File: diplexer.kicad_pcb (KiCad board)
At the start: 2 copper layers, 157 x 72 mm, 27 parts, among them J1 Conn_Coaxial, J2 Conn_Coaxial, J3 Conn_Coaxial, J4 Conn_01x01_Pin, J5 Conn_01x01_Pin, J6 Conn_01x01_Pin, J7 Conn_01x01_Pin

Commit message: Add files via upload
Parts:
- added J10: Conn_01x01_Pin, MountingHole:MountingHole_3.2mm_M3_DIN965_Pad, F.Cu at (133.0, 65.0)
- added J11: Conn_01x01_Pin, MountingHole:MountingHole_3.2mm_M3_DIN965_Pad, F.Cu at (185.0, 65.0)
- added J8: Conn_01x01_Pin, MountingHole:MountingHole_3.2mm_M3_DIN965_Pad, F.Cu at (50.0, 65.0)
- added J9: Conn_01x01_Pin, MountingHole:MountingHole_3.2mm_M3_DIN965_Pad, F.Cu at (92.0, 65.0)
- J4, J5, J6, J7: footprint MountingHole:MountingHole_3.2mm_M3 -> MountingHole:MountingHole_3.2mm_M3_DIN965_Pad
- moved C9 20.6 mm to (137.0, 93.0), turned to 90 degrees
- moved L6 20.0 mm to (139.4, 83.0), turned to 0 degrees
- moved C7 20.0 mm to (86.0, 93.0), turned to 90 degrees
- moved C10 18.7 mm to (166.0, 93.5)
- moved C8 18.4 mm to (116.0, 93.0), turned to 90 degrees
- moved C6 16.6 mm to (67.0, 92.5), turned to 90 degrees
- moved C4 13.1 mm to (122.0, 53.4)
- moved L3 12.7 mm to (110.0, 53.6), turned to 90 degrees
- moved L8 10.3 mm to (91.0, 84.0)
- moved L5 9.56 mm to (151.0, 52.6), turned to 90 degrees
- moved L2 8.66 mm to (76.8, 43.4), turned to 0 degrees
- moved L9 8.34 mm to (77.0, 94.6), turned to 90 degrees
- moved L4 8.11 mm to (120.8, 43.4), turned to 0 degrees
- moved C5 7.75 mm to (139.0, 53.4)
- moved L7 7.72 mm to (127.0, 94.2), turned to 90 degrees
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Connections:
- C1 pad 1: Net-(J1-Ext) -> Net-(J1-In)
- J1 pad 1: GND -> Net-(J1-In)
- J1 pad 2: Net-(J1-Ext) -> GND
- J1 pad 3: (no net) -> GND
- J2 pad 3: (no net) -> GND
- J3 pad 3: (no net) -> GND
- L10 pad 1: Net-(J1-Ext) -> Net-(J1-In)
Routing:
- net Net-(J1-Ext): track 45.8 -> 0.00 mm
- net Net-(J1-In): track 0.00 -> 42.2 mm
- net Net-(C3-Pad2): track 15.4 -> 29.6 mm
- net Net-(C2-Pad2): track 12.4 -> 22.4 mm
- net Net-(J3-In): track 23.5 -> 33.1 mm
- net Net-(C6-Pad2): track 19.0 -> 25.9 mm
- net Net-(C8-Pad2): track 19.8 -> 26.3 mm
- net Net-(C4-Pad2): track 17.5 -> 23.4 mm
- net Net-(J2-In): track 41.2 -> 35.5 mm
- net Net-(C9-Pad2): track 24.5 -> 20.9 mm
- net Net-(C7-Pad2): track 18.3 -> 21.2 mm
- net Net-(C1-Pad2): track 16.7 -> 14.0 mm
- net GND: vias 96 -> 0
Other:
- board text added: "COPPER SHEAT AS SHIELD"
- board text added: "HF+6M lowpass and 4M highpass filter."

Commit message: Add files via upload
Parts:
- added REF**: KiCad-Logo2_8mm_SilkScreen, Symbol:KiCad-Logo2_8mm_SilkScreen, F.Cu at (168.0, 35.0)
- added REF**: OSHW-Logo2_14.6x12mm_SilkScreen, Symbol:OSHW-Logo2_14.6x12mm_SilkScreen, F.Cu at (164.0, 74.0)
- added REF**: Symbol_CreativeCommonsPublicDomain_SilkScreenTop_Small, Symbol:Symbol_CreativeCommonsPublicDomain_SilkScreenTop_Small, F.Cu at (88.0, 72.0)
- moved J9 4.00 mm to (96.0, 65.0)
- moved J10 1.00 mm to (134.0, 65.0)
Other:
- board text added: "1.5MM THICK"
- board text added: "15MM TALL"

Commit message: Add files via upload
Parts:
- moved C3 10.5 mm to (98.0, 53.4)
- moved C5 2.00 mm to (141.0, 53.4)
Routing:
- net Net-(C3-Pad2): track 29.6 -> 19.0 mm
- net Net-(C2-Pad2): track 22.4 -> 32.9 mm
- net Net-(J2-In): track 35.5 -> 33.5 mm
- net Net-(C4-Pad2): track 23.4 -> 25.4 mm
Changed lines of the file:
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@@
 	(footprint "Capacitor_SMD:C_2220_5750Metric"
 		(layer "F.Cu")
-		(at 139 53.44)
+		(at 141 53.44)
 		(descr "Capacitor SMD 2220 (5750 Metric), square (rectangular) end terminal, IPC-7351 nominal, (Body size from: http://datasheets.avx.com/AVX-HV_MLCC.pdf), generated with kicad-footprint-generator")
 		(tags "capacitor")
@@
 		(attr through_hole)
 		(fp_line
-			(start 18.28 -4.87)
+			(start 11.5 -4.87)
 			(end 2.04 -4.87)
 			(stroke
@@
 		)
 		(fp_line
-			(start 19.08 0)
-			(end 18.28 0)
+			(start 12.4 0)
+			(end 11.6 0)
 			(stroke
 				(width 0.12)
@@
 		)
 		(fp_line
-			(start 18.28 4.87)
-			(end 18.28 -4.87)
+			(start 11.5 4.87)
+			(end 11.5 -4.87)
 			(stroke
 				(width 0.12)
@@
 		(fp_line
 			(start 2.04 4.87)
-			(end 18.28 4.87)
-			(stroke
-				(width 0.12)
-				(type solid)
-			)
-			(layer "F.SilkS")
-		)
-		(fp_line
-			(start 21.57 -5)
+			(end 11.5 4.87)
+			(stroke
+				(width 0.12)
+				(type solid)
+			)
+			(layer "F.SilkS")
+		)
+		(fp_line
+			(start 16.5 -5)
 			(end -1.25 -5)
 			(stroke
@@
 		)
 		(fp_line
-			(start 21.57 5)
-			(end 21.57 -5)
+			(start 16.5 5)
+			(end 16.5 -5)
 			(stroke
 				(width 0.05)
@@
 		(fp_line
 			(start -1.25 5)
-			(end 21.57 5)
-			(stroke
-				(width 0.05)
-				(type solid)
-			)
-			(layer "F.CrtYd")
-		)
-		(fp_line
-			(start 18.16 -4.75)
+			(end 16.5 5)
+			(stroke
+				(width 0.05)
+				(type solid)
+			)
+			(layer "F.CrtYd")
+		)
+		(fp_line
+			(start 11.5 -4.75)
 			(end 2.16 -4.75)
 			(stroke
@@
 		)
 		(fp_line
-			(start 20.32 0)
-			(end 18.16 0)
+			(start 13.48 0)
+			(end 11.32 0)
 			(stroke
 				(width 0.1)
@@
 		)
 		(fp_line
-			(start 18.16 4.75)
-			(end 18.16 -4.75)
+			(start 11.5 4.75)
+			(end 11.5 -4.75)
 			(stroke
 				(width 0.1)
@@
 		(fp_line
 			(start 2.16 4.75)
-			(end 18.16 4.75)
+			(end 11.5 4.75)
 			(stroke
 				(width 0.1)
@@
 		(pad "1" thru_hole circle
 			(at 0 0 90)
-			(size 2 2)
-			(drill 1)
+			(size 3 3)
+			(drill 1.6)
 			(layers "*.Cu" "*.Mask")
 			(remove_unused_layers no)
@@
 	(footprint "Capacitor_SMD:C_2220_5750Metric"
 		(layer "F.Cu")
-		(at 87.45 53.44)
+		(at 98 53.44)
 		(descr "Capacitor SMD 2220 (5750 Metric), square (rectangular) end terminal, IPC-7351 nominal, (Body size from: http://datasheets.avx.com/AVX-HV_MLCC.pdf), generated with kicad-footprint-generator")
 		(tags "capacitor")
@@
 	)
 	(segment
-		(start 84.9 53.44)
-		(end 76.84 53.44)
-		(width 3)
-		(layer "F.Cu")
-		(net 3)
-	)
-	(segment
 		(start 76.84 53.44)
 		(end 72.55 53.44)
+		(width 3)
+		(layer "F.Cu")
+		(net 3)
+	)
+	(segment
+		(start 95.45 53.44)
+		(end 76.84 53.44)
 		(width 3)
 		(layer "F.Cu")
@@
 	)
 	(segment
+		(start 100.55 53.44)
+		(end 109.84 53.44)
+		(width 3)
+		(layer "F.Cu")
+		(net 4)
+	)
+	(segment
 		(start 119.29 53.6)
 		(end 110 53.6)
@@
 	)
 	(segment
-		(start 110 53.6)
-		(end 90.16 53.6)
-		(width 3)
-		(layer "F.Cu")
-		(net 4)
-	)
-	(segment
-		(start 90.16 53.6)
-		(end 90 53.44)
+		(start 109.84 53.44)
+		(end 110 53.6)
 		(width 3)
 		(layer "F.Cu")
@@
 	)
 	(segment
-		(start 136.45 53.44)
-		(end 124.55 53.44)
-		(width 3)
-		(layer "F.Cu")
-		(net 5)
-	)
-	(segment
 		(start 124.55 47.15)
 		(end 120.84 43.44)
+		(width 3)
+		(layer "F.Cu")
+		(net 5)
+	)
+	(segment
+		(start 138.45 53.44)
+		(end 124.55 53.44)
 		(width 3)
 		(layer "F.Cu")
@@
 	)
 	(segment
+		(start 143.55 53.44)
+		(end 144.39 52.6)
+		(width 3)
+		(layer "F.Cu")
+		(net 6)
+	)
+	(segment
 		(start 151 52.6)
 		(end 169.4 52.6)
@@
 	)
 	(segment
-		(start 142.39 52.6)
+		(start 144.39 52.6)
 		(end 151 52.6)
 		(width 3)
 		(layer "F.Cu")
-		(net 6)
-	)
-	(segment
-		(start 141.55 53.44)
-		(end 142.39 52.6)
-		(width 3)
-		(layer "F.Cu")

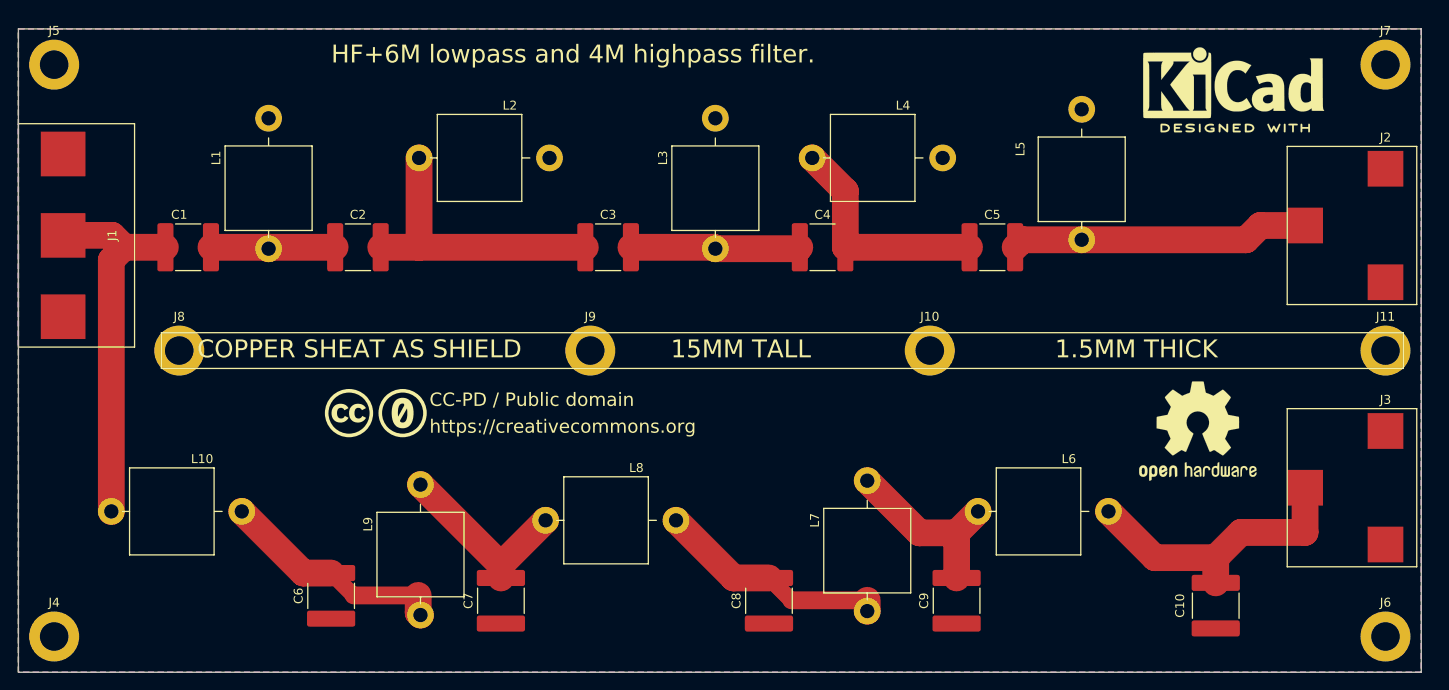
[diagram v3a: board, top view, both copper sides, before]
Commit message: Add files via upload
Updated capacitors foot prints to 2525 (QEEV Series)
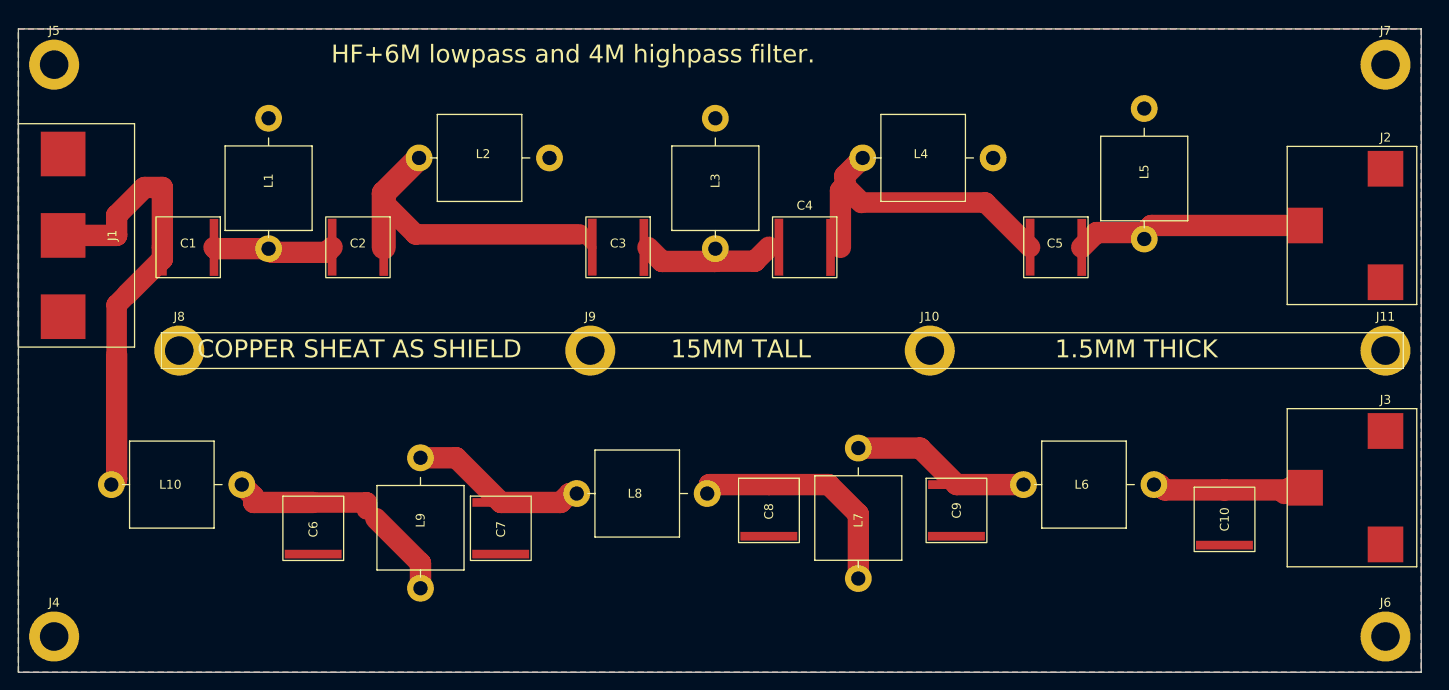
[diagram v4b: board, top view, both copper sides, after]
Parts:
- removed REF**: KiCad-Logo2_8mm_SilkScreen, Symbol:KiCad-Logo2_8mm_SilkScreen
- removed REF**: OSHW-Logo2_14.6x12mm_SilkScreen, Symbol:OSHW-Logo2_14.6x12mm_SilkScreen
- removed REF**: Symbol_CreativeCommonsPublicDomain_SilkScreenTop_Small, Symbol:Symbol_CreativeCommonsPublicDomain_SilkScreenTop_Small
- C1, C10, C2, C3, C4, C5, C6, C7, C8, C9: footprint Capacitor_SMD:C_2220_5750Metric -> sparkfun-electromech:2525
- moved C9 10.1 mm to (137.0, 82.9), turned to 0 degrees
- moved C8 10.1 mm to (116.0, 82.9), turned to 0 degrees
- moved C10 9.71 mm to (167.0, 83.9), turned to 0 degrees
- moved C7 8.11 mm to (86.0, 84.9), turned to 0 degrees
- moved C6 7.82 mm to (65.0, 84.9), turned to 0 degrees
- moved C5 7.11 mm to (148.1, 53.4), turned to -90 degrees
- moved L5 7.00 mm to (158.0, 52.5)
- moved L6 5.91 mm to (144.5, 80.0)
- moved L4 5.65 mm to (126.5, 43.4)
- moved L8 4.60 mm to (94.5, 81.0)
- moved L7 3.78 mm to (126.0, 90.5)
- moved L10 3.00 mm to (42.4, 80.0)
- moved L9 3.00 mm to (77.0, 91.6)
- moved C4 2.00 mm to (120.0, 53.4), turned to -90 degrees
- moved C3 1.11 mm to (99.1, 53.4), turned to -90 degrees
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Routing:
- net Net-(J3-In): track 33.1 -> 17.4 mm
- net Net-(C4-Pad2): track 25.4 -> 34.6 mm
- net Net-(J1-In): track 42.2 -> 50.3 mm
- net Net-(J2-In): track 33.5 -> 26.7 mm
- net Net-(C2-Pad2): track 32.9 -> 37.0 mm
- net Net-(C3-Pad2): track 19.0 -> 16.3 mm
- net Net-(C6-Pad2): track 25.9 -> 27.3 mm
- net Net-(C7-Pad2): track 21.2 -> 20.0 mm
- net Net-(C9-Pad2): track 20.9 -> 20.2 mm

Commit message: Add files via upload
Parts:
- added C11: 30pF, sparkfun-electromech:1111, F.Cu at (51.2, 48.1)
- added C12: 12pF, sparkfun-electromech:1111, F.Cu at (70.0, 48.0)
- added C13: 12pF, sparkfun-electromech:1111, F.Cu at (99.0, 48.0)
- added C14: 12pF, sparkfun-electromech:1111, F.Cu at (120.0, 48.0)
- added C15: 10pF, sparkfun-electromech:1111, F.Cu at (148.0, 49.0)
- added C16: 16pF, sparkfun-electromech:1111, F.Cu at (69.0, 86.0)
- added C17: 10pF, sparkfun-electromech:1111, F.Cu at (91.0, 86.0)
- added C18: 10pF, sparkfun-electromech:1111, F.Cu at (120.0, 84.0)
- added C19: 10pF, sparkfun-electromech:1111, F.Cu at (141.0, 84.0)
- added C20: 22pF, sparkfun-electromech:1111, F.Cu at (170.5, 83.5)
- C1: value 43pF -> 13pF; footprint sparkfun-electromech:2525 -> sparkfun-electromech:1111
- C10: value 62pF -> 39pF; footprint sparkfun-electromech:2525 -> sparkfun-electromech:1111
- C2, C4: value 24pF -> 12pF; footprint sparkfun-electromech:2525 -> sparkfun-electromech:1111
- C3: value 24F -> 12pF; footprint sparkfun-electromech:2525 -> sparkfun-electromech:1111
- C5: value 30pF -> 20pF; footprint sparkfun-electromech:2525 -> sparkfun-electromech:1111
- C6: value 91pF -> 75pF; footprint sparkfun-electromech:2525 -> sparkfun-electromech:1111
- C7, C9: value 110pF -> 100pF; footprint sparkfun-electromech:2525 -> sparkfun-electromech:1111
- C8: value 110ppF -> 100pF; footprint sparkfun-electromech:2525 -> sparkfun-electromech:1111
- moved C10 3.75 mm to (163.5, 82.5)
- moved C6 2.90 mm to (62.1, 84.9)
- moved C8 2.00 mm to (114.0, 83.0)
- moved C9 1.99 mm to (135.0, 82.9)
- moved L7 1.50 mm to (127.5, 90.5)
- moved C7 0.89 mm to (85.1, 84.9)
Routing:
- net Net-(C13-Pad2): track 16.3 -> 30.0 mm
- net Net-(C1-Pad2): track 13.7 -> 26.0 mm
- net Net-(C12-Pad2): track 37.0 -> 45.6 mm
- net Net-(C14-Pad2): track 34.6 -> 40.9 mm
- net Net-(J2-In): track 26.7 -> 32.4 mm
- net Net-(J3-In): track 17.4 -> 22.9 mm
- net Net-(J1-In): track 50.3 -> 45.5 mm
- net Net-(C17-Pad1): track 20.0 -> 23.3 mm
- net Net-(C18-Pad1): track 26.3 -> 25.0 mm
- net Net-(C19-Pad1): track 20.2 -> 21.2 mm
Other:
- board text added: "100W MAX!"

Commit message: Add files via upload
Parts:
- J2: footprint sparkfun-electromech:N-conn slanted -> sparkfun-electromech:UHF slanted
- moved J2 1.90 mm to (184.0, 49.4), turned to 90 degrees
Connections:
- net Net-(J2-In) renamed /HF+6M
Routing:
- net /HF+6M: track 32.4 -> 41.1 mm

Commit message: Add files via upload
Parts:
- J2: footprint sparkfun-electromech:UHF slanted -> sparkfun-electromech:N-conn slanted
- J3: footprint sparkfun-electromech:N-conn slanted -> sparkfun-electromech:UHF slanted
- turned J2 to -90 degrees
- turned J3 to 90 degrees
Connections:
- net /HF+6M renamed Net-(J2-In)
- J1 pad 3: GND -> (no net)
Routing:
- net Net-(J3-In): track 22.9 -> 31.9 mm
- net Net-(J2-In): track 41.1 -> 32.1 mm
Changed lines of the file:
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@@
 	(net 10 "Net-(C18-Pad1)")
 	(net 11 "Net-(C19-Pad1)")
-	(net 12 "/HF+6M")
+	(net 12 "Net-(J2-In)")
 	(footprint "sparkfun-electromech:1111"
 		(layer "F.Cu")
@@
 		)
 	)
-	(footprint "sparkfun-electromech:N-conn slanted"
+	(footprint "sparkfun-electromech:UHF slanted"
 		(layer "F.Cu")
-		(at 185 80.35 -90)
+		(at 185 80.35 90)
+		(descr "UHF slanted")
 		(property "Reference" "J3"
-			(at -9.85 0 0)
+			(at 0 -5.5 90)
 			(layer "F.SilkS")
 			(effects
@@
 			)
 		)
-		(property "Footprint" "sparkfun-electromech:N-conn slanted"
+		(property "Footprint" "sparkfun-electromech:UHF slanted"
 			(at 0 0 90)
 			(layer "F.Fab")
@@
 		(attr smd)
 		(fp_line
-			(start -8.85 11)
-			(end -8.85 -3.5)
+			(start 12.5 -8)
+			(end -12.5 -8)
 			(stroke
 				(width 0.12)
@@
 		)
 		(fp_line
-			(start 8.85 11)
-			(end -8.85 11)
+			(start -12.5 -8)
+			(end -12.5 5)
 			(stroke
 				(width 0.12)
@@
 		)
 		(fp_line
-			(start -8.85 -3.5)
-			(end 8.85 -3.5)
+			(start 12.5 5)
+			(end 12.5 -8)
 			(stroke
 				(width 0.12)
@@
 		)
 		(fp_line
-			(start 8.85 -3.5)
-			(end 8.85 11)
+			(start -12.5 5)
+			(end 12.5 5)
 			(stroke
 				(width 0.12)
@@
 		)
 		(fp_line
-			(start -8.6 10.5)
-			(end -8.6 -3)
+			(start 12 -3)
+			(end 12 4.5)
 			(stroke
 				(width 0.05)
@@
 		)
 		(fp_line
-			(start 8.6 10.5)
-			(end -8.6 10.5)
+			(start -12 -3)
+			(end 12 -3)
 			(stroke
 				(width 0.05)
@@
 		)
 		(fp_line
-			(start -8.6 -3)
-			(end 8.6 -3)
+			(start 12 4.5)
+			(end -12 4.5)
 			(stroke
 				(width 0.05)
@@
 		)
 		(fp_line
-			(start 8.6 -3)
-			(end 8.6 10.5)
+			(start -12 4.5)
+			(end -12 -3)
 			(stroke
 				(width 0.05)
@@
 		)
 		(pad "1" smd rect
-			(at 0 9 270)
-			(size 4 4)
+			(at 0 0 90)
+			(size 5 5)
 			(layers "F.Cu" "F.Paste" "F.Mask")
 			(net 4 "Net-(J3-In)")
@@
 		)
 		(pad "2" smd rect
-			(at -6.35 0 270)
-			(size 4 4)
+			(at -9.11 0 90)
+			(size 5 5)
 			(layers "F.Cu" "F.Paste" "F.Mask")
 			(net 3 "GND")
 			(pinfunction "Ext")
 			(pintype "passive")
-			(thermal_bridge_angle 45)
 		)
 		(pad "3" smd rect
-			(at 6.35 0 270)
-			(size 4 4)
+			(at 9.1 0 90)
+			(size 5 5)
 			(layers "F.Cu" "F.Paste" "F.Mask")
 			(net 3 "GND")
-			(thermal_bridge_angle 45)
 		)
 	)
@@
 		)
 	)
-	(footprint "sparkfun-electromech:UHF slanted"
+	(footprint "sparkfun-electromech:N-conn slanted"
 		(layer "F.Cu")
-		(at 184 49.39 90)
-		(descr "UHF slanted")
+		(at 184 49.39 -90)
 		(property "Reference" "J2"
-			(at 0 -5.5 90)
+			(at -9.85 0 360)
 			(layer "F.SilkS")
 			(effects
@@
 			)
 		)
-		(property "Footprint" "sparkfun-electromech:UHF slanted"
+		(property "Footprint" "sparkfun-electromech:N-conn slanted"
 			(at 0 0 90)
 			(layer "F.Fab")
@@
 		(attr smd)
 		(fp_line
-			(start 12.5 -8)
-			(end -12.5 -8)
+			(start -8.85 11)
+			(end -8.85 -3.5)
 			(stroke
 				(width 0.12)
@@
 		)
 		(fp_line
-			(start -12.5 -8)
-			(end -12.5 5)
+			(start 8.85 11)
+			(end -8.85 11)
 			(stroke
 				(width 0.12)
@@
 		)
 		(fp_line
-			(start 12.5 5)
-			(end 12.5 -8)
+			(start -8.85 -3.5)
+			(end 8.85 -3.5)
 			(stroke
 				(width 0.12)
@@
 		)
 		(fp_line
-			(start -12.5 5)
-			(end 12.5 5)
+			(start 8.85 -3.5)
+			(end 8.85 11)
 			(stroke
 				(width 0.12)
@@
 		)
 		(fp_line
-			(start 12 -3)
-			(end 12 4.5)
+			(start -8.6 10.5)
+			(end -8.6 -3)
 			(stroke
 				(width 0.05)
@@
 		)
 		(fp_line
-			(start -12 -3)
-			(end 12 -3)
+			(start 8.6 10.5)
+			(end -8.6 10.5)
 			(stroke
 				(width 0.05)
@@
 		)
 		(fp_line
-			(start 12 4.5)
-			(end -12 4.5)
+			(start -8.6 -3)
+			(end 8.6 -3)
 			(stroke
 				(width 0.05)
@@
 		)
 		(fp_line
-			(start -12 4.5)
-			(end -12 -3)
+			(start 8.6 -3)
+			(end 8.6 10.5)
 			(stroke
 				(width 0.05)
@@
 		)
 		(pad "1" smd rect
-			(at 0 0 90)
-			(size 5 5)
+			(at 0 9 270)
+			(size 4 4)
 			(layers "F.Cu" "F.Paste" "F.Mask")
-			(net 12 "/HF+6M")
+			(net 12 "Net-(J2-In)")
 			(pinfunction "In")
 			(pintype "passive")
@@
 		)
 		(pad "2" smd rect
-			(at -9.11 0 90)
-			(size 5 5)
+			(at -6.35 0 270)
+			(size 4 4)
 			(layers "F.Cu" "F.Paste" "F.Mask")
 			(net 3 "GND")
 			(pinfunction "Ext")
 			(pintype "passive")
+			(thermal_bridge_angle 45)
 		)
 		(pad "3" smd rect
-			(at 9.1 0 90)
-			(size 5 5)
+			(at 6.35 0 270)
+			(size 4 4)
 			(layers "F.Cu" "F.Paste" "F.Mask")
 			(net 3 "GND")
+			(thermal_bridge_angle 45)
 		)
 	)
@@
 			(size 1.78 1.78)
 			(layers "F.Cu" "F.Paste" "F.Mask")
-			(net 12 "/HF+6M")
+			(net 12 "Net-(J2-In)")
 			(pintype "passive")
 			(thermal_bridge_angle 45)
@@
 			(size 5 5)
 			(layers "F.Cu" "F.Paste" "F.Mask")
-			(net 3 "GND")
 		)
 	)
@@
 			(size 1.78 1.78)
 			(layers "F.Cu" "F.Paste" "F.Mask")
-			(net 12 "/HF+6M")
+			(net 12 "Net-(J2-In)")
 			(pintype "passive")
 			(thermal_bridge_angle 45)
@@
 			(layers "*.Cu" "*.Mask")
 			(remove_unused_layers no)
-			(net 12 "/HF+6M")
+			(net 12 "Net-(J2-In)")
 			(pinfunction "1")
 			(pintype "passive")
@@
 	)
 	(segment
-		(start 176 80.35)
-		(end 174.4617 80.35)
+		(start 173.9867 80.825)
+		(end 169.6 80.825)
 		(width 2.39)
 		(layer "F.Cu")
@@
 	)
 	(segment
+		(start 174.4617 80.35)
+		(end 173.9867 80.825)
+		(width 2.39)
+		(layer "F.Cu")
+		(net 4)
+	)
+	(segment
 		(start 159.3133 80)
 		(end 160.0133 80.7)
@@
 	)
 	(segment
-		(start 168.7852 80)
-		(end 169.6 80.8148)
-		(width 2.39)
-		(layer "F.Cu")
-		(net 4)
-	)
-	(segment
-		(start 174.4617 80.35)
-		(end 173.9867 80.825)
+		(start 185 80.35)
+		(end 174.4617 80.35)
 		(width 2.39)
 		(layer "F.Cu")
@@
 	)
 	(segment
-		(start 169.6 80.825)
-		(end 173.9867 80.825)
+		(start 168.7852 80)
+		(end 169.6 80.8148)
 		(width 2.39)
 		(layer "F.Cu")
@@
 	)
 	(segment
-		(start 159.5125 51)
-		(end 158 52.5125)
-		(width 2.39)
-		(layer "F.Cu")
-		(net 12)
-	)
-	(segment
 		(start 149.8 49.9)
 		(end 154.1867 49.9)
@@
 	)
 	(segment
-		(start 184 49.39)
-		(end 182.39 51)
+		(start 159.5125 51)
+		(end 158 52.5125)
 		(width 2.39)
 		(layer "F.Cu")
@@
 	)
 	(segment
-		(start 182.39 51)
+		(start 173.39 51)
 		(end 159.5125 51)
 		(width 2.39)
 		(layer "F.Cu")
+		(net 12)
+	)
+	(segment
+		(start 175 49.39)
+		(end 173.39 51)
+		(width 2.39)
+		(layer "F.Cu")
